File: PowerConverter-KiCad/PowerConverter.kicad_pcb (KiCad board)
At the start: 4 copper layers, 99.1 x 99.1 mm, 55 parts, among them J1 3220-10-0100-00, J2 Conn_01x03_Pin, Q1 IRFB7430PBF, U1 UCC27517AQDBVRQ1, U2 STM32G431RBTx, U3 AP63205, U4 AMS1117-3.3, Y1 16MHz

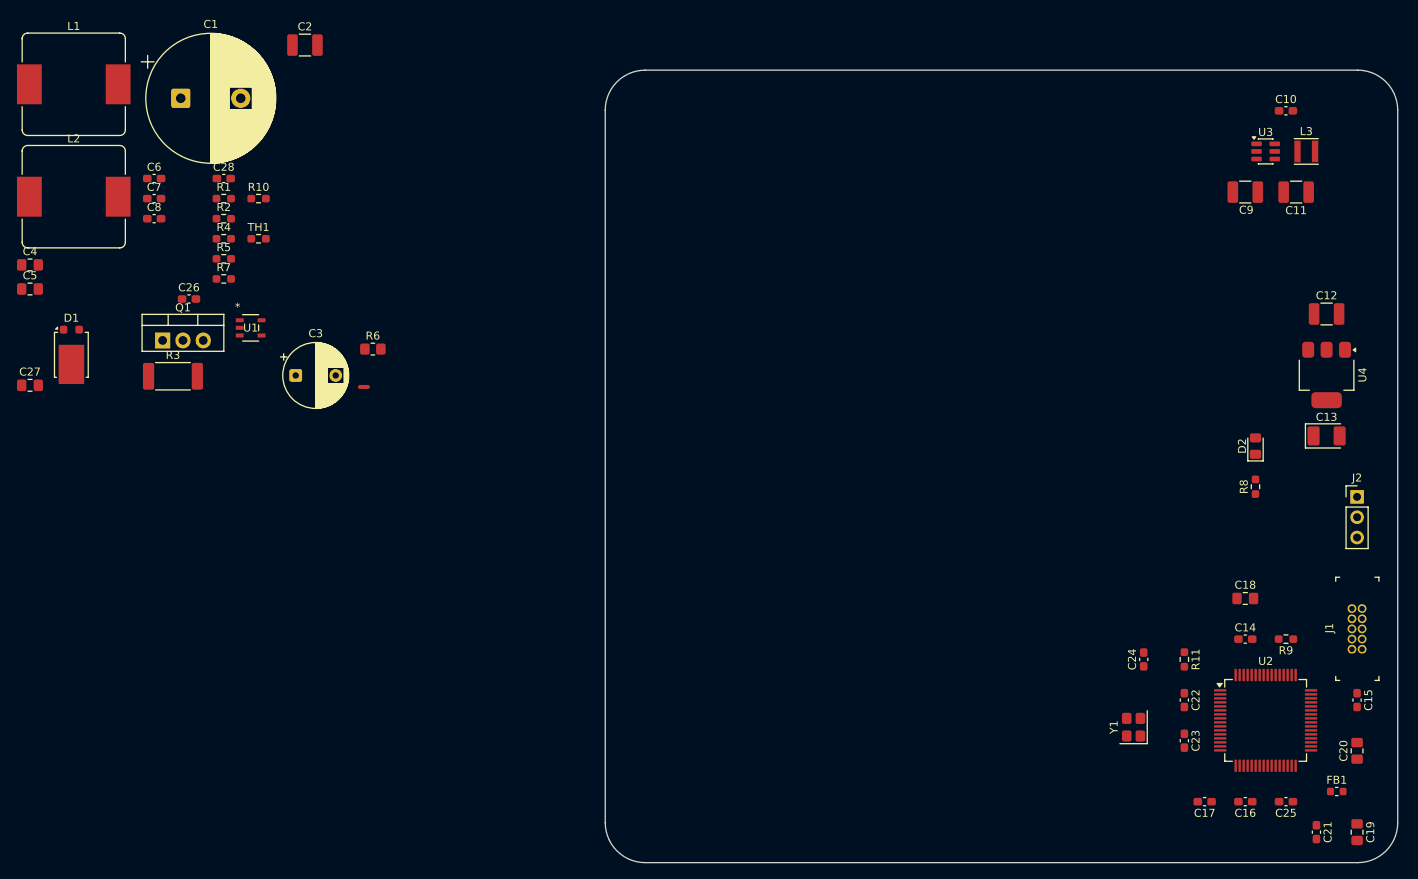
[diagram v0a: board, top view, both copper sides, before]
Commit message: SEPIC v2.0: 4-Layer Stackup, 12V Power Plane on In2, and High Current Via Stitching implemented
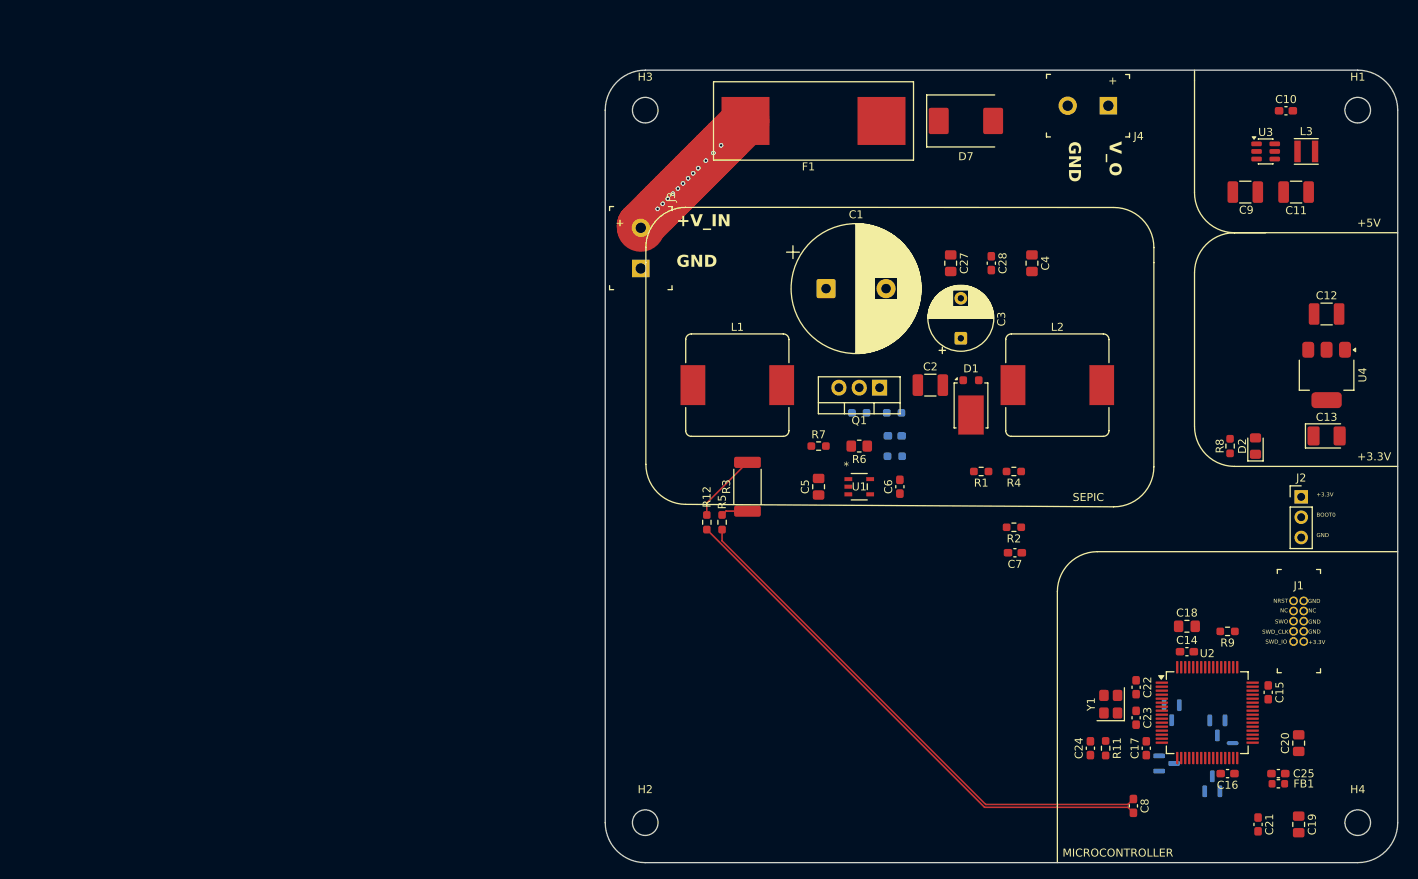
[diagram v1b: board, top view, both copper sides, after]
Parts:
- added D3: BAT54S, Package_TO_SOT_SMD:SOT-23, B.Cu at (161.0, 105.7)
- added D4: BAT54S, Package_TO_SOT_SMD:SOT-23, B.Cu at (166.7, 107.6)
- added D5: BAT54S, Package_TO_SOT_SMD:SOT-23, B.Cu at (166.1, 114.6)
- added D6: BAT54S, Package_TO_SOT_SMD:SOT-23, B.Cu at (160.3, 112.1)
- added D7: SMAJ15A, Diode_SMD:D_SMC, F.Cu at (135.3, 31.8)
- added F1: Fuse, Fuse:Fuseholder_Cylinder-5x20mm_Wuerth_696103101002-SMD_Horizontal_Open, F.Cu at (116.2, 31.8)
- added H1: MountingHole, MountingHole:MountingHole_3.2mm_M3, F.Cu at (184.2, 30.4)
- added H2: MountingHole, MountingHole:MountingHole_3.2mm_M3, F.Cu at (95.2, 119.5)
- added H3: MountingHole, MountingHole:MountingHole_3.2mm_M3, F.Cu at (95.2, 30.4)
- added H4: MountingHole, MountingHole:MountingHole_3.2mm_M3, F.Cu at (184.2, 119.5)
- added J3: Screw_Terminal_01x02, digikey-footprints:Term_Block_1x2_P5.08MM, F.Cu at (94.6, 50.2)
- added J4: Screw_Terminal_01x02, digikey-footprints:Term_Block_1x2_P5.08MM, F.Cu at (153.1, 29.8)
- added R12: 1k, Resistor_SMD:R_0603_1608Metric_Pad0.98x0.95mm_HandSolder, F.Cu at (102.9, 81.9)
- added R13: 1k, Resistor_SMD:R_0603_1608Metric_Pad0.98x0.95mm_HandSolder, B.Cu at (126.4, 73.7)
- C26, NT1, R10, TH1: moved to B.Cu
- R5: value 100 -> 1k
- U3: value AP63205 -> AP63205WU
- moved C8 142.7 mm to (156.2, 117.4), turned to -90 degrees
- moved C4 125.2 mm to (143.5, 49.5), turned to -90 degrees
- moved L2 125.2 mm to (146.7, 64.8)
- moved NT1 117.4 mm to (168.6, 109.5), turned to 180 degrees
- moved C7 116.3 mm to (141.4, 85.7), turned to 180 degrees
- moved C27 116.1 mm to (133.3, 49.5), turned to -90 degrees
- moved D1 112.6 mm to (135.9, 67.3)
- moved R2 106.0 mm to (141.3, 82.5), turned to 180 degrees
- moved R4 103.0 mm to (141.2, 75.6), turned to 180 degrees
- moved C5 101.6 mm to (116.8, 77.5), turned to 90 degrees
- moved C6 100.9 mm to (127.0, 77.5), turned to 90 degrees
- moved R1 100.6 mm to (137.2, 75.6), turned to 180 degrees
- moved C28 96.5 mm to (138.4, 49.5), turned to -90 degrees
- moved L1 91.1 mm to (106.7, 64.8)
- moved C26 89.9 mm to (126.4, 71.1)
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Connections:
- net /PA7 renamed /I_SENSE_P
- C1 pad 1: +12V -> /Vi_1
- C26 pad 1: /PB2 -> Net-(C26-Pad1)
- C27 pad 1: +12V -> /Vi_1
- C28 pad 1: +12V -> /Vi_1
- C8 pad 2: GNDA -> /I_SENSE_N
- L1 pad 1: +12V -> /Vi_1
- R10 pad 1: /PB2 -> Net-(C26-Pad1)
- TH1 pad 1: /PB2 -> Net-(C26-Pad1)
- U2 pad 19: unconnected-(U2-PA5-Pad19) -> /I_SENSE_N
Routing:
- net /I_SENSE_N: track 0.00 -> 68.0 mm
- net /I_SENSE_P: track 0.00 -> 66.8 mm
- net +12V: track 0.00 -> 18.8 mm, vias 0 -> 12
- net GND: track 0.00 -> 8.69 mm
- net /Source: track 0.00 -> 3.37 mm
- added copper zone on In2.Cu, net +12V
- added copper zone on In1.Cu, net GND
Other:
- board text added: "+"
- board text added: "+3.3V"
- board text added: "+5V"
- board text added: "+V_IN"
- board text added: "BOOT0"
- board text added: "GND"
- board text added: "MICROCONTROLLER"
- board text added: "NC"
- board text added: "NRST"
- board text added: "SEPIC"
- board text added: "SWD_CLK"
- board text added: "SWD_IO"
- board text added: "SWO"
- board text added: "V_O"

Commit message: Layout update: PA8 bottom layer shielding, U1 RC filter optimization, VDDA daisy-chain routing, and via-in-pad corrections
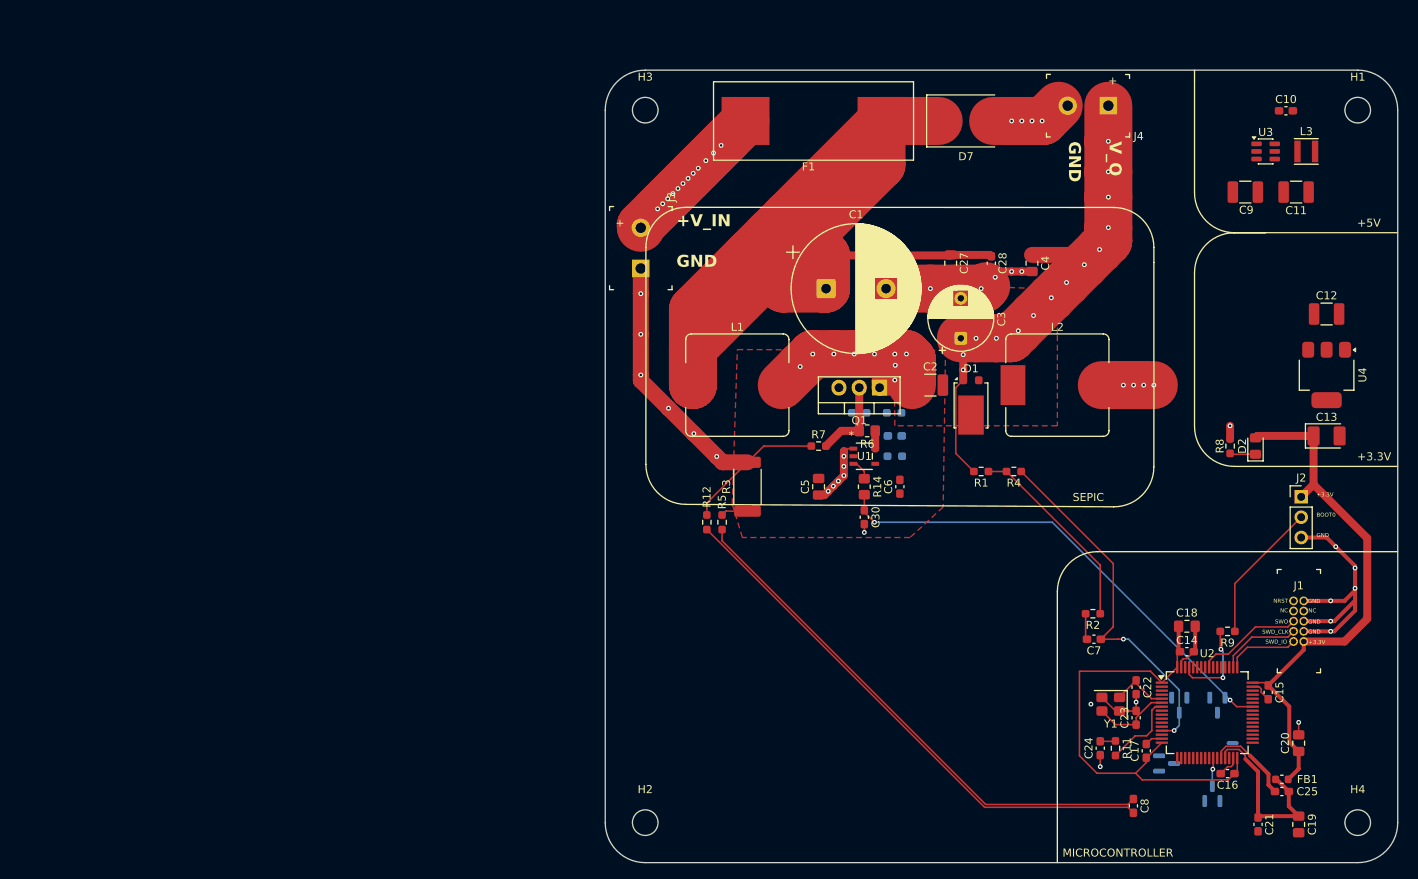
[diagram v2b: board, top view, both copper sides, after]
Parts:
- added C30: 1nF, Capacitor_SMD:C_0603_1608Metric_Pad1.08x0.95mm_HandSolder, F.Cu at (122.6, 81.3)
- added R14: 10, Resistor_SMD:R_0805_2012Metric_Pad1.20x1.40mm_HandSolder, F.Cu at (122.6, 77.5)
- moved C7 14.6 mm to (151.3, 96.5)
- moved R2 14.6 mm to (151.1, 93.3)
- moved U1 3.86 mm to (122.6, 73.7)
- moved D4 2.84 mm to (166.7, 104.8)
- moved C25 2.28 mm to (174.8, 115.6)
- moved R6 2.15 mm to (122.9, 70.5)
- moved D3 1.33 mm to (161.9, 104.8)
- moved C24 1.23 mm to (152.0, 110.2)
- moved R11 1.23 mm to (153.9, 110.2)
- moved D5 1.22 mm to (166.1, 115.8)
- moved FB1 0.71 mm to (174.8, 114.0)
- moved C17 0.33 mm to (157.8, 110.5)
- turned C23 to 90 degrees
- turned Y1 to 180 degrees
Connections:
- net /Vi_1 renamed Net-(D7-A1)
- U1 pad 3: /PA8 -> Net-(U1-IN+)
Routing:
- net Net-(D7-A1): track 0.00 -> 139.6 mm
- net GND: track 8.69 -> 146.2 mm, vias 0 -> 33
- net +3.3V: track 0.00 -> 125.7 mm
- net /V_O2: track 0.00 -> 65.5 mm, vias 0 -> 14
- net /PA8: track 0.00 -> 60.8 mm, vias 0 -> 2
- net /PA1: track 0.00 -> 45.7 mm, vias 0 -> 2
- net /SW_NODE: track 0.00 -> 34.8 mm, vias 0 -> 9
- net Net-(R1-Pad1): track 0.00 -> 24.9 mm
- net +3.3VA: track 0.00 -> 23.2 mm
- net Net-(J2-Pin_2): track 0.00 -> 17.7 mm
- net /SWO: track 0.00 -> 13.4 mm
- net /BOOT0: track 0.00 -> 11.2 mm, vias 0 -> 2
- net Net-(U2-VREF+): track 0.00 -> 11.0 mm
- net /Gate: track 0.00 -> 10.4 mm
- net /SWDCLK: track 0.00 -> 10.2 mm
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- added copper zone on In2.Cu, net /SW_NODE
- added copper zone on F.Cu, net /Source
- added copper zone on F.Cu, net /V_O1
- added copper zone on In2.Cu, net /V_O2
